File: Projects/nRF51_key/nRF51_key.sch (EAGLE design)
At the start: 14 parts, among them IC1 FT230XQ, J1 47571-0001, X1 USBPCB

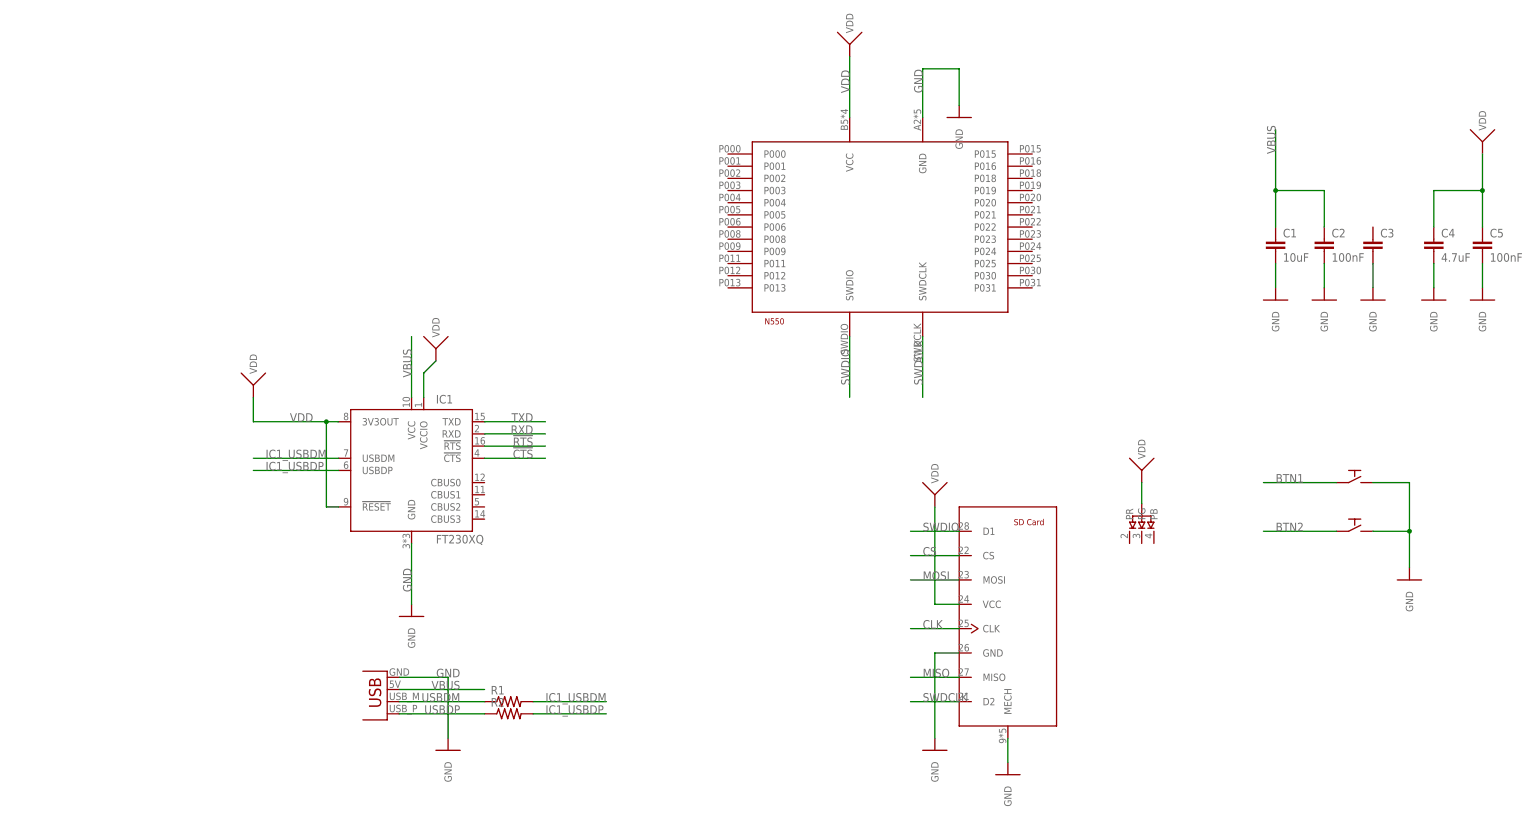
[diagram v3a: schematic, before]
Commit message: Added buttons on ZLL Added pads on nRF51 key SD prog finished N5 lib updated
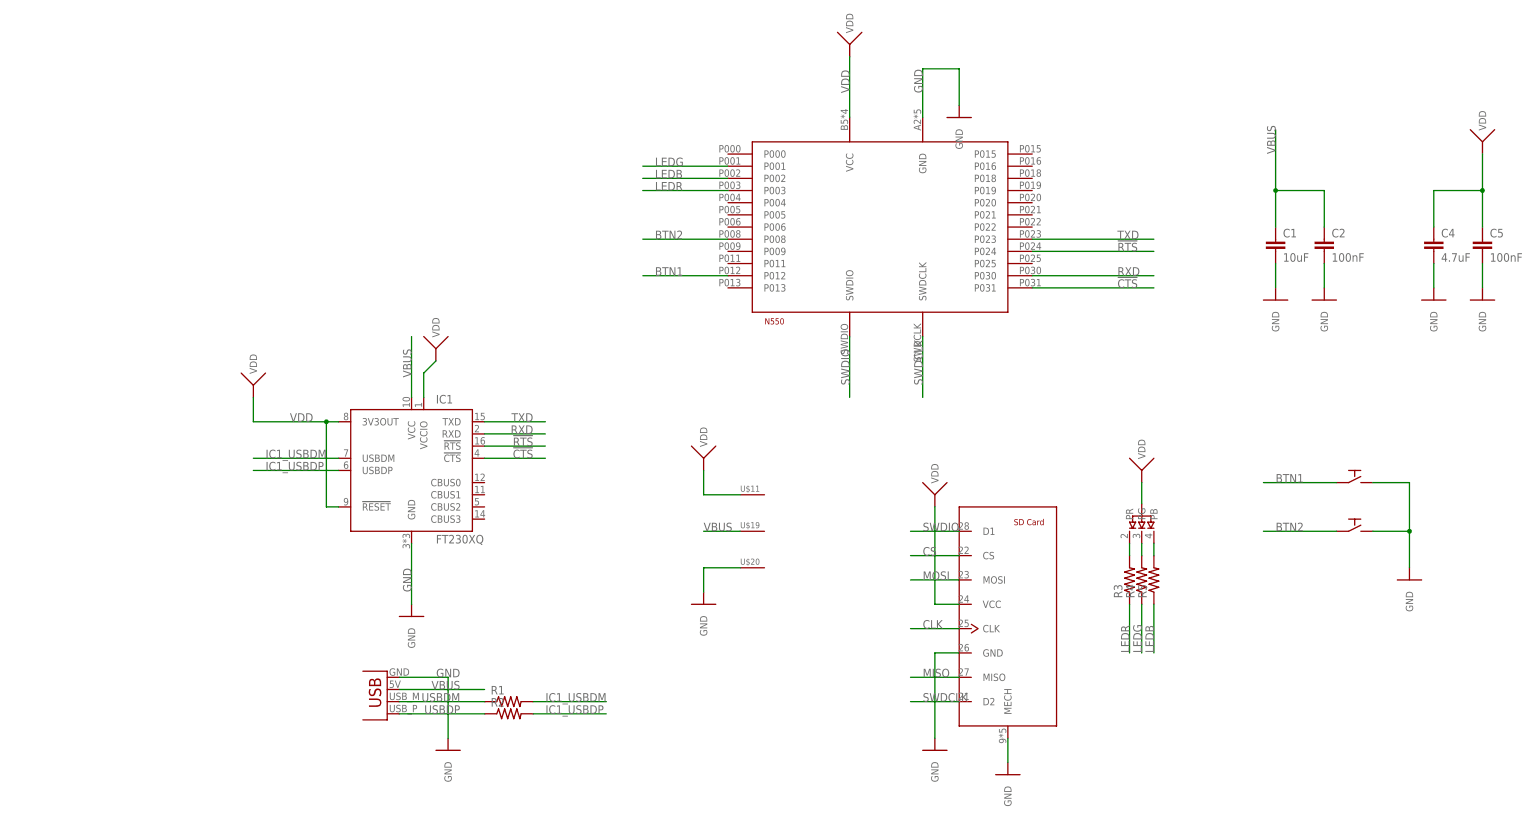
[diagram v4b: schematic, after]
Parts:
- removed C3: (no value), Passives:CAPACITOR0603
- added R3, R4, R5: (no value), Passives:RESISTOR0603
- added U$11, U$19, U$20: PAD, ParanoidStudio:PAD
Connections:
- new net LEDB: R5.1, U$1.P002
- new net LEDG: R4.1, U$1.P001
- new net LEDR: R3.1, U$1.P003
- new net N$1: D1.PR, R3.2
- new net N$2: D1.PG, R4.2
- new net N$3: D1.PB, R5.2
- net !CTS: now also U$1.P031
- net !RTS: now also U$1.P024
- net BTN1: now also U$1.P012
- net BTN2: now also U$1.P008
- net GND: now also U$20.P$1; no longer C3.2
- net RXD: now also U$1.P030
- net TXD: now also U$1.P023
- net VBUS: now also U$19.P$1
- net VDD: now also U$11.P$1

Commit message: nRF51 dongle with new pins
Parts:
- added U$23, U$24, U$25, U$26: PAD, ParanoidStudio:PAD
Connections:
- net !CTS: now also U$26.P$1
- net !RTS: now also U$25.P$1
- net CLK: now also U$1.P013
- net CS: now also U$1.P011
- net MISO: now also U$1.P018
- net MOSI: now also U$1.P015
- net RXD: now also U$24.P$1
- net TXD: now also U$23.P$1
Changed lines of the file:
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@@
 </variantdefs>
 <classes>
-<class number="0" name="default" width="0.1524" drill="0.762">
+<class number="0" name="default" width="0.1524" drill="0.3">
 <clearance class="0" value="0.1524"/>
 </class>
@@
 <part name="U$21" library="PowerSupplies" deviceset="VDD" device=""/>
 <part name="U$22" library="PowerSupplies" deviceset="GND" device=""/>
+<part name="U$23" library="ParanoidStudio" deviceset="PAD" device=""/>
+<part name="U$24" library="ParanoidStudio" deviceset="PAD" device=""/>
+<part name="U$25" library="ParanoidStudio" deviceset="PAD" device=""/>
+<part name="U$26" library="ParanoidStudio" deviceset="PAD" device=""/>
 </parts>
 <sheets>
@@
 <instance part="U$21" gate="G$1" x="5.08" y="-20.32" smashed="yes"/>
 <instance part="U$22" gate="GND" x="5.08" y="-50.8" smashed="yes"/>
+<instance part="U$23" gate="G$1" x="104.14" y="25.4" smashed="yes">
+<attribute name="NAME" x="99.06" y="26.035" size="1.27" layer="95"/>
+</instance>
+<instance part="U$24" gate="G$1" x="104.14" y="17.78" smashed="yes">
+<attribute name="NAME" x="99.06" y="18.415" size="1.27" layer="95"/>
+</instance>
+<instance part="U$25" gate="G$1" x="104.14" y="22.86" smashed="yes">
+<attribute name="NAME" x="99.06" y="23.495" size="1.27" layer="95"/>
+</instance>
+<instance part="U$26" gate="G$1" x="104.14" y="15.24" smashed="yes">
+<attribute name="NAME" x="99.06" y="15.875" size="1.27" layer="95"/>
+</instance>
 </instances>
 <busses>
@@
 <wire x1="73.66" y1="15.24" x2="99.06" y2="15.24" width="0.1524" layer="91"/>
 <label x="91.44" y="15.24" size="1.778" layer="95"/>
+<pinref part="U$26" gate="G$1" pin="P$1"/>
 </segment>
 </net>
@@
 <wire x1="73.66" y1="22.86" x2="99.06" y2="22.86" width="0.1524" layer="91"/>
 <label x="91.44" y="22.86" size="1.778" layer="95"/>
+<pinref part="U$25" gate="G$1" pin="P$1"/>
 </segment>
 </net>
@@
 <wire x1="73.66" y1="17.78" x2="99.06" y2="17.78" width="0.1524" layer="91"/>
 <label x="91.44" y="17.78" size="1.778" layer="95"/>
+<pinref part="U$24" gate="G$1" pin="P$1"/>
 </segment>
 </net>
@@
 <wire x1="73.66" y1="25.4" x2="99.06" y2="25.4" width="0.1524" layer="91"/>
 <label x="91.44" y="25.4" size="1.778" layer="95"/>
+<pinref part="U$23" gate="G$1" pin="P$1"/>
 </segment>
 </net>
@@
 <label x="50.8" y="-66.04" size="1.778" layer="95"/>
 </segment>
+<segment>
+<pinref part="U$1" gate="G$1" pin="P018"/>
+<wire x1="73.66" y1="38.1" x2="99.06" y2="38.1" width="0.1524" layer="91"/>
+<label x="91.44" y="38.1" size="1.778" layer="95"/>
+</segment>
 </net>
 <net name="CLK" class="0">
@@
 <label x="50.8" y="-55.88" size="1.778" layer="95"/>
 </segment>
+<segment>
+<pinref part="U$1" gate="G$1" pin="P013"/>
+<wire x1="10.16" y1="15.24" x2="-7.62" y2="15.24" width="0.1524" layer="91"/>
+<label x="-5.08" y="15.24" size="1.778" layer="95"/>
+</segment>
 </net>
 <net name="MOSI" class="0">
@@
 <label x="50.8" y="-45.72" size="1.778" layer="95"/>
 </segment>
+<segment>
+<pinref part="U$1" gate="G$1" pin="P015"/>
+<wire x1="73.66" y1="43.18" x2="99.06" y2="43.18" width="0.1524" layer="91"/>
+<label x="91.44" y="43.18" size="1.778" layer="95"/>
+</segment>
 </net>
 <net name="CS" class="0">
@@
 <label x="50.8" y="-40.64" size="1.778" layer="95"/>
 </segment>
-</net>
+<segment>
+<pinref part="U$1" gate="G$1" pin="P011"/>
+<wire x1="10.16" y1="20.32" x2="-7.62" y2="20.32" width="0.1524" layer="91"/>
+<label x="-5.08" y="20.32" size="1.778" layer="95"/>
+</segment>
+</net>
